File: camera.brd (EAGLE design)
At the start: 42.5 x 38.1 mm, 10 parts

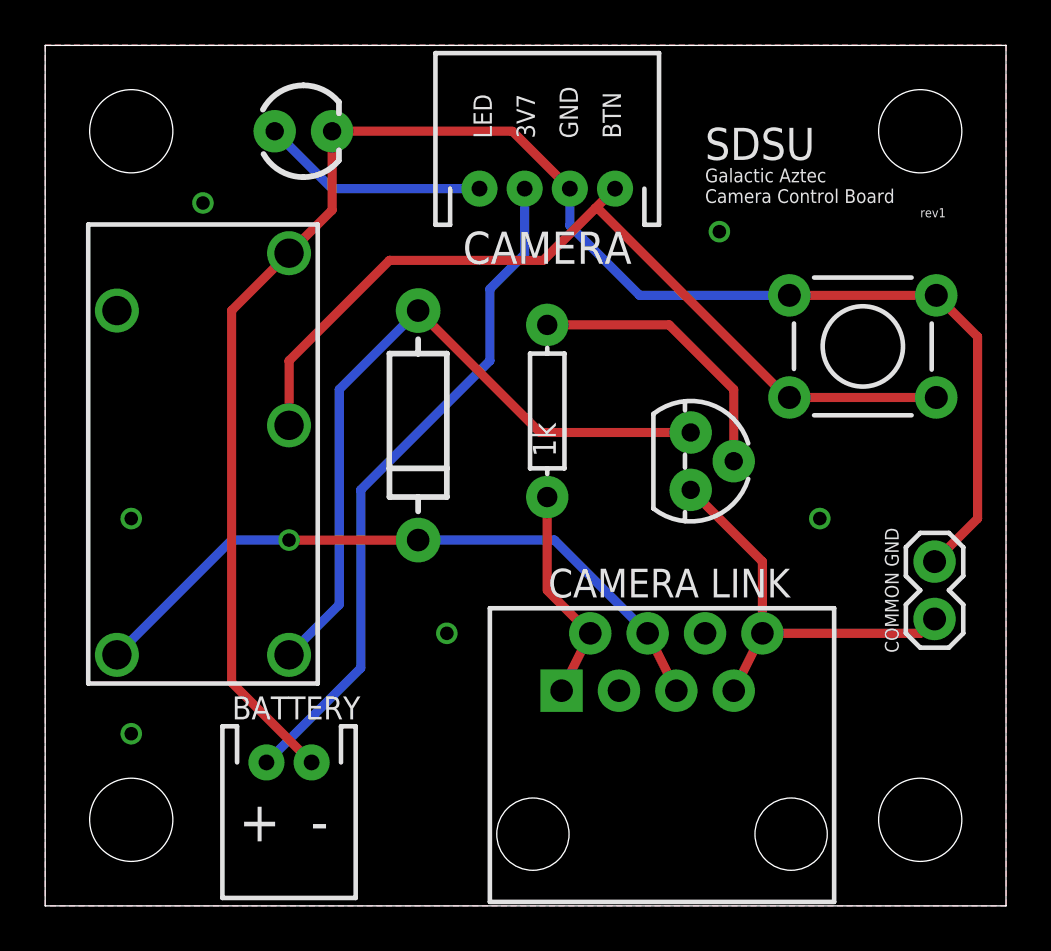
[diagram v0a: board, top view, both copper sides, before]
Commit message: Significantly reduce board footprint
Significant reduction in board footprint as the result of moving relay
and related electronic components to the supporting Galactic Aztec RPi
Add-on: Valve + Camera Control board.
Components that remain on this board were replaced with SMD versions.
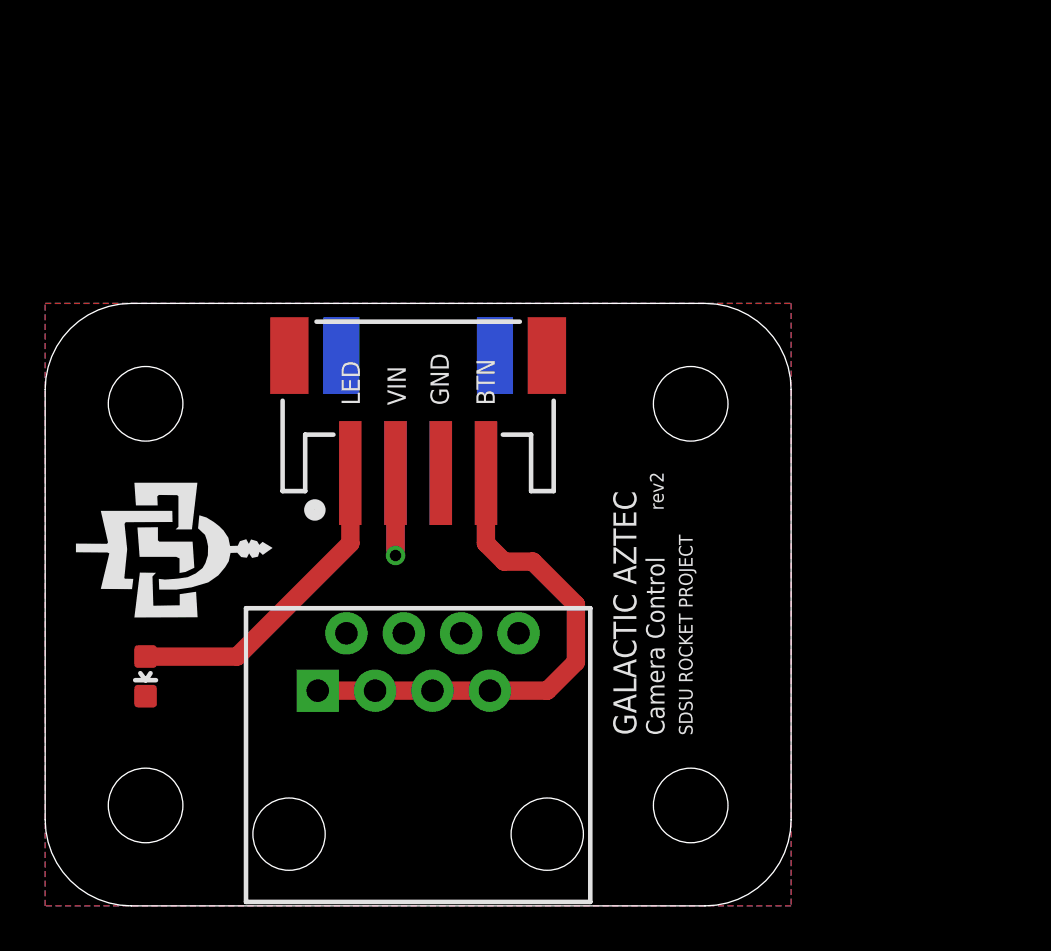
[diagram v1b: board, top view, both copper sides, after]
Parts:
- removed D3: (no value), SparkFun-DiscreteSemi:DIODE-1N4001
- removed JP3: CAMERA, SparkFun-Connectors:JST-4-PTH
- removed Q3: (no value), SparkFun-DiscreteSemi:TO-92
- removed R3: 1k, SparkFun-Resistors:AXIAL-0.3
- removed S1: (no value), SparkFun-Electromechanical:TACTILE-PTH
- added CN1: (no value), microbuilder_v2:JSTPH4
- added FRAME1: (no value), SparkFun-Aesthetics:CREATIVE_COMMONS
- added U$1, U$2: (no value), SparkFun-Electromechanical:STAND-OFF
- JP1: value COMMON GND -> RJ45; device SparkFun-Connectors:1X02 -> SparkFun-Connectors:RJ45-8
- JP11: device SparkFun-Connectors:JST-2-PTH -> SparkFun-Connectors:JST-2-SMD
- LED1: value (none) -> GREEN; device SparkFun-LED:LED3MM -> SparkFun-LED:LED-0603
- U$3: value CAMERA -> (none); device SparkFun-Electromechanical:RELAY-G5Q -> SparkFun-Electromechanical:STAND-OFF
- U$4: value CAMERA CONTROL -> (none); device SparkFun-Connectors:RJ45-8 -> SparkFun-Electromechanical:STAND-OFF
- moved U$3 26.6 mm to (28.6, 4.45), turned to 0 degrees
- moved JP1 25.8 mm to (16.5, 3.17), turned to 0 degrees
- moved LED1 25.1 mm to (4.45, 10.2), turned to 180 degrees
- moved U$4 19.1 mm to (28.6, 22.2)
- moved JP11 17.5 mm to (16.5, 22.9), flipped to the bottom, turned to 0 degrees
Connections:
- removed net 3V7: JP11.2, JP3.2
- removed net 5V: D3.C, U$3.5, U$4.4, U$4.5
- removed net BUTTON: JP3.4, S1.1, S1.2, U$3.2
- removed net CGND: JP1.1, JP11.1, JP3.3, LED1.K, S1.3, S1.4, U$3.3
- removed net N$11: D3.A, Q3.1, U$3.1
- removed net N$5: Q3.2, R3.P$2
- removed net SIG: R3.P$1, U$4.1, U$4.2
- new net PIN3: CN1.4, JP1.1, JP1.3, JP1.5, JP1.7
- new net VIN: CN1.2, JP11.2
- net GND: now also CN1.3, JP1.4, JP1.6, JP1.8, JP11.1, LED1.C; no longer Q3.3, U$4.7, U$4.8
- net LED: now also CN1.1; no longer JP3.1
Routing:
- net CGND: track 75.3 -> 0.00 mm, vias 5 -> 0
- net BUTTON: track 39.0 -> 0.00 mm
- net N$11: track 31.9 -> 0.00 mm
- net 5V: track 30.1 -> 0.00 mm, vias 1 -> 0
- net 3V7: track 30.1 -> 0.00 mm
- net PIN3: track 0.00 -> 22.7 mm
- net GND: track 18.4 -> 0.00 mm
- net N$5: track 12.6 -> 0.00 mm
- net SIG: track 9.66 -> 0.00 mm
- net VIN: track 0.00 -> 7.30 mm, vias 0 -> 1
- net LED: track 10.1 -> 14.3 mm
- added copper zone on layer 1, net GND
- added copper zone on layer 16, net GND
- removed copper zone on layer 1, net CGND
- removed copper zone on layer 16, net CGND
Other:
- board size 42.5 x 38.1 mm -> 33 x 26.7 mm
- board text added: "Camera Control"
- board text added: "GALACTIC AZTEC"
- board text added: "SDSU ROCKET PROJECT"
- board text added: "VIN"
- board text added: "rev2"
- board text added: "ø0.13"
- board text removed: "+"
- board text removed: "-"
- board text removed: "3V7"
- board text removed: "BATTERY"
- board text removed: "CAMERA"
- board text removed: "CAMERA LINK"
- board text removed: "Galactic Aztec Camera Control Board"
- board text removed: "SDSU"
- board text removed: "rev1"
